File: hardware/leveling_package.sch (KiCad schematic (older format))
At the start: 3 parts, among them J1 Conn_01x16_Male, J2 Conn_01x16_Male

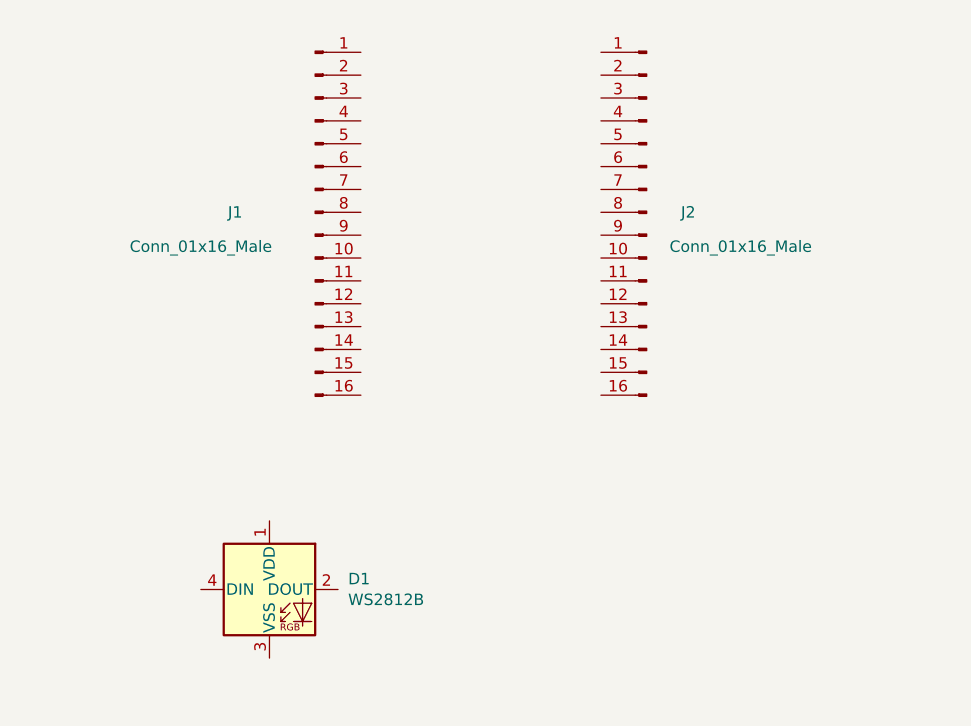
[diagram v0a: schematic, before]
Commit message: first leg with all leds
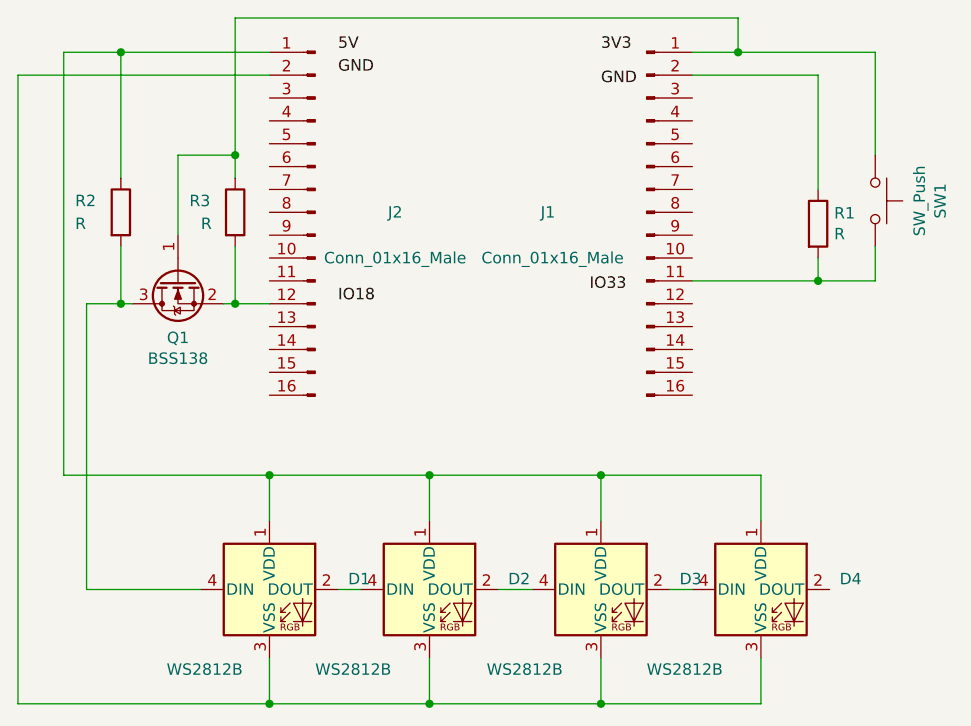
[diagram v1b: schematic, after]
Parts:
- added D2, D3, D4: WS2812B, LED_SMD:LED_WS2812B_PLCC4_5.0x5.0mm_P3.2mm, symbol LED:WS2812B
- added Q1: BSS138, Package_TO_SOT_SMD:SOT-23, symbol Transistor_FET:BSS138
- added R1, R2, R3: R, Resistor_SMD:R_0805_2012Metric_Pad1.15x1.40mm_HandSolder, symbol Device:R
- added SW1: SW_Push, Button_Switch_THT:SW_PUSH_6mm, symbol Switch:SW_Push
- renumbered J2 to J1, J1 to J2
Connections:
- net at J2.1 (Pin_1): now also D1.1 (VDD), D2.1 (VDD), D3.1 (VDD), D4.1 (VDD), R2.1
- net at J2.12 (Pin_12): now also Q1.2 (S), R3.2
- net at J2.2 (Pin_2): now also D1.3 (VSS), D2.3 (VSS), D3.3 (VSS), D4.3 (VSS)
- net at J1.1 (Pin_1): now also Q1.1 (G), R3.1, SW1.1
- net at J1.11 (Pin_11): now also R1.2, SW1.2
- net at J1.2 (Pin_2): now also R1.1
- net at D1.2 (DOUT): now also D2.4 (DIN)
- net at D1.4 (DIN): now also Q1.3 (D), R2.2
- new net: D2.2 (DOUT), D3.4 (DIN)
- new net: D3.2 (DOUT), D4.4 (DIN)
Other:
- moved on the sheet: J1, J2
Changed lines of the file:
@@
 $EndDescr
 $Comp
-L Connector:Conn_01x16_Male J1
+L Connector:Conn_01x16_Male J2
 U 1 1 603EA836
 P 3650 3350
-F 0 "J1" H 3300 3350 50  0000 C CNN
-F 1 "Conn_01x16_Male" H 3150 3200 50  0000 C CNN
+F 0 "J2" H 3300 3350 50  0000 C CNN
+F 1 "Conn_01x16_Male" H 3300 3150 50  0000 C CNN
 F 2 "Connector_PinHeader_2.54mm:PinHeader_1x16_P2.54mm_Vertical" H 3650 3350 50  0001 C CNN
 F 3 "~" H 3650 3350 50  0001 C CNN
 	1    3650 3350
-	1    0    0    -1
-$EndComp
-$Comp
-L Connector:Conn_01x16_Male J2
+	-1   0    0    -1
+$EndComp
+$Comp
+L Connector:Conn_01x16_Male J1
 U 1 1 603ECB79
 P 5100 3350
-F 0 "J2" H 4950 3350 50  0000 R CNN
-F 1 "Conn_01x16_Male" H 5000 3200 50  0000 R CNN
+F 0 "J1" H 4700 3350 50  0000 R CNN
+F 1 "Conn_01x16_Male" H 5000 3150 50  0000 R CNN
 F 2 "Connector_PinHeader_2.54mm:PinHeader_1x16_P2.54mm_Vertical" H 5100 3350 50  0001 C CNN
 F 3 "~" H 5100 3350 50  0001 C CNN
 	1    5100 3350
-	-1   0    0    -1
+	1    0    0    -1
 $EndComp
 $Comp
@@
 P 3450 5000
 F 0 "D1" H 3794 5046 50  0000 L CNN
-F 1 "WS2812B" H 3794 4955 50  0000 L CNN
+F 1 "WS2812B" H 3000 4650 50  0000 L CNN
 F 2 "LED_SMD:LED_WS2812B_PLCC4_5.0x5.0mm_P3.2mm" H 3500 4700 50  0001 L TNN
 F 3 "https://cdn-shop.adafruit.com/datasheets/WS2812B.pdf" H 3550 4625 50  0001 L TNN
@@
 	1    0    0    -1
 $EndComp
+$Comp
+L Switch:SW_Push SW1
+U 1 1 603FB7A3
+P 6100 3300
+F 0 "SW1" H 6100 3585 50  0000 C CNN
+F 1 "SW_Push" H 6100 3494 50  0000 C CNN
+F 2 "Button_Switch_THT:SW_PUSH_6mm" H 6100 3500 50  0001 C CNN
+F 3 "~" H 6100 3500 50  0001 C CNN
+	1    6100 3300
+	0    1    1    0
+$EndComp
+$Comp
+L Device:R R1
+U 1 1 603F0D7F
+P 5850 3400
+F 0 "R1" H 5920 3446 50  0000 L CNN
+F 1 "R" H 5920 3355 50  0000 L CNN
+F 2 "Resistor_SMD:R_0805_2012Metric_Pad1.15x1.40mm_HandSolder" V 5780 3400 50  0001 C CNN
+F 3 "~" H 5850 3400 50  0001 C CNN
+	1    5850 3400
+	1    0    0    -1
+$EndComp
+Wire Wire Line
+	5300 3650 5850 3650
+Wire Wire Line
+	5850 3650 5850 3550
+Wire Wire Line
+	5850 3250 5850 2750
+Wire Wire Line
+	5850 2750 5300 2750
+Wire Wire Line
+	5850 3650 6100 3650
+Wire Wire Line
+	6100 3650 6100 3500
+Connection ~ 5850 3650
+Wire Wire Line
+	6100 3100 6100 2650
+Wire Wire Line
+	6100 2650 5500 2650
+Wire Wire Line
+	3450 4700 3450 4500
+Wire Wire Line
+	3450 4500 2550 4500
+Wire Wire Line
+	2550 4500 2550 2650
+Wire Wire Line
+	2550 2650 2800 2650
+Wire Wire Line
+	3450 5300 3450 5500
+Wire Wire Line
+	3450 5500 2350 5500
+Wire Wire Line
+	2350 5500 2350 2750
+Wire Wire Line
+	2350 2750 3450 2750
+$Comp
+L Transistor_FET:BSS138 Q1
+U 1 1 6040B788
+P 3050 3650
+F 0 "Q1" V 3299 3650 50  0000 C CNN
+F 1 "BSS138" V 3390 3650 50  0000 C CNN
+F 2 "Package_TO_SOT_SMD:SOT-23" H 3250 3575 50  0001 L CIN
+F 3 "https://www.fairchildsemi.com/datasheets/BS/BSS138.pdf" H 3050 3650 50  0001 L CNN
+	1    3050 3650
+	0    -1   1    0
+$EndComp
+Text Label 4900 2650 0    50   ~ 0
+3V3
+Text Label 3750 2650 0    50   ~ 0
+5V
+Text Label 3750 2750 0    50   ~ 0
+GND
+Text Label 4900 2800 0    50   ~ 0
+GND
+Text Label 4850 3700 0    50   ~ 0
+IO33
+Text Label 3750 3750 0    50   ~ 0
+IO18
+Wire Wire Line
+	3450 3750 3300 3750
+Wire Wire Line
+	3150 5000 2650 5000
+Wire Wire Line
+	2650 5000 2650 3750
+Wire Wire Line
+	2650 3750 2800 3750
+$Comp
+L Device:R R3
+U 1 1 6043545A
+P 3300 3350
+F 0 "R3" H 3100 3400 50  0000 L CNN
+F 1 "R" H 3150 3300 50  0000 L CNN
+F 2 "Resistor_SMD:R_0805_2012Metric_Pad1.15x1.40mm_HandSolder" V 3230 3350 50  0001 C CNN
+F 3 "~" H 3300 3350 50  0001 C CNN
+	1    3300 3350
+	1    0    0    -1
+$EndComp
+Wire Wire Line
+	3300 3500 3300 3750
+Connection ~ 3300 3750
+Wire Wire Line
+	3300 3750 3250 3750
+Wire Wire Line
+	3300 3200 3300 3100
+Wire Wire Line
+	3300 2500 5500 2500
+Wire Wire Line
+	5500 2500 5500 2650
+Connection ~ 5500 2650
+Wire Wire Line
+	5500 2650 5300 2650
+Wire Wire Line
+	3300 3100 3050 3100
+Wire Wire Line
+	3050 3100 3050 3450
+Connection ~ 3300 3100
+Wire Wire Line
+	3300 3100 3300 2500
+$Comp
+L Device:R R2
+U 1 1 604443A8
+P 2800 3350
+F 0 "R2" H 2600 3400 50  0000 L CNN
+F 1 "R" H 2600 3300 50  0000 L CNN
+F 2 "Resistor_SMD:R_0805_2012Metric_Pad1.15x1.40mm_HandSolder" V 2730 3350 50  0001 C CNN
+F 3 "~" H 2800 3350 50  0001 C CNN
+	1    2800 3350
+	1    0    0    -1
+$EndComp
+Wire Wire Line
+	2800 3500 2800 3750
+Connection ~ 2800 3750
+Wire Wire Line
+	2800 3750 2850 3750
+Wire Wire Line
+	2800 3200 2800 2650
+Connection ~ 2800 2650
+Wire Wire Line
+	2800 2650 3450 2650
+$Comp
+L LED:WS2812B D2
+U 1 1 60457101
+P 4150 5000
+F 0 "D2" H 4494 5046 50  0000 L CNN
+F 1 "WS2812B" H 3650 4650 50  0000 L CNN
+F 2 "LED_SMD:LED_WS2812B_PLCC4_5.0x5.0mm_P3.2mm" H 4200 4700 50  0001 L TNN
+F 3 "https://cdn-shop.adafruit.com/datasheets/WS2812B.pdf" H 4250 4625 50  0001 L TNN
+	1    4150 5000
+	1    0    0    -1
+$EndComp
+Wire Wire Line
+	3750 5000 3850 5000
+Wire Wire Line
+	3450 5500 4150 5500
+Wire Wire Line
+	4150 5500 4150 5300
+Connection ~ 3450 5500
+Wire Wire Line
+	3450 4500 4150 4500
+Wire Wire Line
+	4150 4500 4150 4700
+Connection ~ 3450 4500
+$Comp
+L LED:WS2812B D3
+U 1 1 6045C053
+P 4900 5000
+F 0 "D3" H 5244 5046 50  0000 L CNN
+F 1 "WS2812B" H 4400 4650 50  0000 L CNN
+F 2 "LED_SMD:LED_WS2812B_PLCC4_5.0x5.0mm_P3.2mm" H 4950 4700 50  0001 L TNN
+F 3 "https://cdn-shop.adafruit.com/datasheets/WS2812B.pdf" H 5000 4625 50  0001 L TNN
+	1    4900 5000
+	1    0    0    -1
+$EndComp
+Wire Wire Line
+	4150 4500 4900 4500
+Wire Wire Line
+	4900 4500 4900 4700
+Connection ~ 4150 4500
+Wire Wire Line
+	4900 5300 4900 5500
+Wire Wire Line
+	4900 5500 4150 5500
+Connection ~ 4150 5500
+Wire Wire Line
+	4450 5000 4600 5000
+$Comp
+L LED:WS2812B D4
+U 1 1 6045F1B5
+P 5600 5000
+F 0 "D4" H 5944 5046 50  0000 L CNN
+F 1 "WS2812B" H 5100 4650 50  0000 L CNN
+F 2 "LED_SMD:LED_WS2812B_PLCC4_5.0x5.0mm_P3.2mm" H 5650 4700 50  0001 L TNN
+F 3 "https://cdn-shop.adafruit.com/datasheets/WS2812B.pdf" H 5700 4625 50  0001 L TNN
+	1    5600 5000
+	1    0    0    -1
+$EndComp
+Wire Wire Line
+	5600 4700 5600 4500
+Wire Wire Line
+	5600 4500 4900 4500
+Connection ~ 4900 4500
+Wire Wire Line
+	5600 5300 5600 5500
+Wire Wire Line
+	5600 5500 4900 5500
+Connection ~ 4900 5500
+Wire Wire Line
+	5200 5000 5300 5000
 $EndSCHEMATC

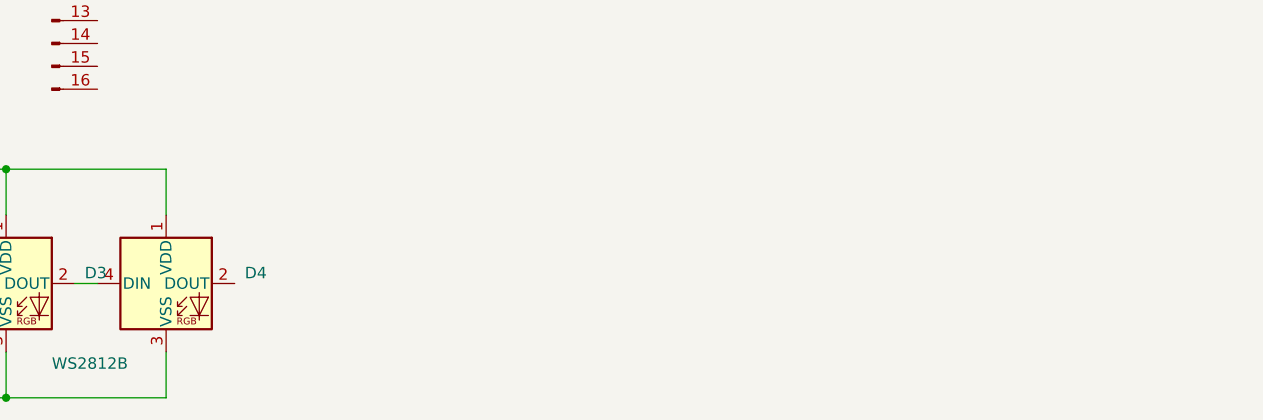
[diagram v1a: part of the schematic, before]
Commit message: all legs with leds
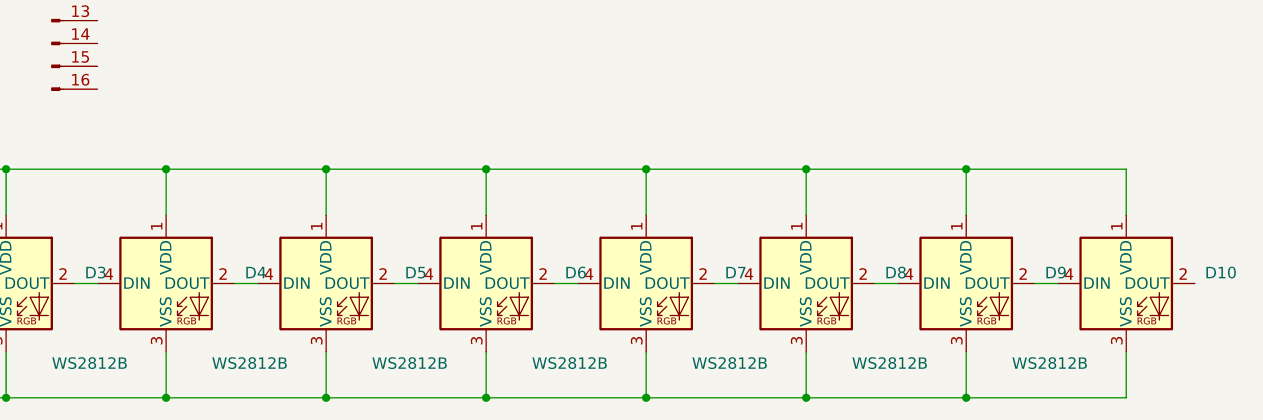
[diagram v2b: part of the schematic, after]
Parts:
- added D10, D5, D6, D7, D8, D9: WS2812B, LED_SMD:LED_WS2812B_PLCC4_5.0x5.0mm_P3.2mm, symbol LED:WS2812B
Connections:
- net at D1.1 (VDD), D2.1 (VDD), D3.1 (VDD)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: now also D10.1 (VDD), D5.1 (VDD), D6.1 (VDD), D7.1 (VDD), D8.1 (VDD), D9.1 (VDD)
- net at D1.3 (VSS), D2.3 (VSS), D3.3 (VSS)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: now also D10.3 (VSS), D5.3 (VSS), D6.3 (VSS), D7.3 (VSS), D8.3 (VSS), D9.3 (VSS)
- net at D4.2 (DOUT): now also D5.4 (DIN)
- new net: D5.2 (DOUT), D6.4 (DIN)
- new net: D6.2 (DOUT), D7.4 (DIN)
- new net: D7.2 (DOUT), D8.4 (DIN)
- new net: D8.2 (DOUT), D9.4 (DIN)
- new net: D10.4 (DIN), D9.2 (DOUT)
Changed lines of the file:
@@
 Wire Wire Line
 	5200 5000 5300 5000
+$Comp
+L LED:WS2812B D5
+U 1 1 604660BC
+P 6300 5000
+F 0 "D5" H 6644 5046 50  0000 L CNN
+F 1 "WS2812B" H 5800 4650 50  0000 L CNN
+F 2 "LED_SMD:LED_WS2812B_PLCC4_5.0x5.0mm_P3.2mm" H 6350 4700 50  0001 L TNN
+F 3 "https://cdn-shop.adafruit.com/datasheets/WS2812B.pdf" H 6400 4625 50  0001 L TNN
+	1    6300 5000
+	1    0    0    -1
+$EndComp
+Wire Wire Line
+	6300 5300 6300 5500
+Wire Wire Line
+	6300 5500 5600 5500
+Connection ~ 5600 5500
+Wire Wire Line
+	6300 4700 6300 4500
+Wire Wire Line
+	6300 4500 5600 4500
+Connection ~ 5600 4500
+Wire Wire Line
+	5900 5000 6000 5000
+$Comp
+L LED:WS2812B D6
+U 1 1 60469B4E
+P 7000 5000
+F 0 "D6" H 7344 5046 50  0000 L CNN
+F 1 "WS2812B" H 6500 4650 50  0000 L CNN
+F 2 "LED_SMD:LED_WS2812B_PLCC4_5.0x5.0mm_P3.2mm" H 7050 4700 50  0001 L TNN
+F 3 "https://cdn-shop.adafruit.com/datasheets/WS2812B.pdf" H 7100 4625 50  0001 L TNN
+	1    7000 5000
+	1    0    0    -1
+$EndComp
+Wire Wire Line
+	7000 4700 7000 4500
+Wire Wire Line
+	7000 4500 6300 4500
+Connection ~ 6300 4500
+Wire Wire Line
+	7000 5500 6300 5500
+Wire Wire Line
+	7000 5300 7000 5500
+Connection ~ 6300 5500
+Wire Wire Line
+	6600 5000 6700 5000
+$Comp
+L LED:WS2812B D7
+U 1 1 6047025A
+P 7700 5000
+F 0 "D7" H 8044 5046 50  0000 L CNN
+F 1 "WS2812B" H 7200 4650 50  0000 L CNN
+F 2 "LED_SMD:LED_WS2812B_PLCC4_5.0x5.0mm_P3.2mm" H 7750 4700 50  0001 L TNN
+F 3 "https://cdn-shop.adafruit.com/datasheets/WS2812B.pdf" H 7800 4625 50  0001 L TNN
+	1    7700 5000
+	1    0    0    -1
+$EndComp
+Wire Wire Line
+	7700 4700 7700 4500
+Wire Wire Line
+	7700 4500 7000 4500
+Connection ~ 7000 4500
+Wire Wire Line
+	7700 5300 7700 5500
+Wire Wire Line
+	7700 5500 7000 5500
+Connection ~ 7000 5500
+Wire Wire Line
+	7300 5000 7400 5000
+$Comp
+L LED:WS2812B D8
+U 1 1 604746C9
+P 8400 5000
+F 0 "D8" H 8744 5046 50  0000 L CNN
+F 1 "WS2812B" H 7900 4650 50  0000 L CNN
+F 2 "LED_SMD:LED_WS2812B_PLCC4_5.0x5.0mm_P3.2mm" H 8450 4700 50  0001 L TNN
+F 3 "https://cdn-shop.adafruit.com/datasheets/WS2812B.pdf" H 8500 4625 50  0001 L TNN
+	1    8400 5000
+	1    0    0    -1
+$EndComp
+Wire Wire Line
+	8400 4700 8400 4500
+Wire Wire Line
+	8400 4500 7700 4500
+Connection ~ 7700 4500
+Wire Wire Line
+	8400 5300 8400 5500
+Wire Wire Line
+	8400 5500 7700 5500
+Connection ~ 7700 5500
+Wire Wire Line
+	8000 5000 8100 5000
+$Comp
+L LED:WS2812B D9
+U 1 1 60480BC4
+P 9100 5000
+F 0 "D9" H 9444 5046 50  0000 L CNN
+F 1 "WS2812B" H 8600 4650 50  0000 L CNN
+F 2 "LED_SMD:LED_WS2812B_PLCC4_5.0x5.0mm_P3.2mm" H 9150 4700 50  0001 L TNN
+F 3 "https://cdn-shop.adafruit.com/datasheets/WS2812B.pdf" H 9200 4625 50  0001 L TNN
+	1    9100 5000
+	1    0    0    -1
+$EndComp
+Wire Wire Line
+	9100 5300 9100 5500
+Wire Wire Line
+	9100 5500 8400 5500
+Connection ~ 8400 5500
+Wire Wire Line
+	9100 4700 9100 4500
+Wire Wire Line
+	9100 4500 8400 4500
+Connection ~ 8400 4500
+Wire Wire Line
+	8700 5000 8800 5000
+$Comp
+L LED:WS2812B D10
+U 1 1 6048635F
+P 9800 5000
+F 0 "D10" H 10144 5046 50  0000 L CNN
+F 1 "WS2812B" H 9300 4650 50  0000 L CNN
+F 2 "LED_SMD:LED_WS2812B_PLCC4_5.0x5.0mm_P3.2mm" H 9850 4700 50  0001 L TNN
+F 3 "https://cdn-shop.adafruit.com/datasheets/WS2812B.pdf" H 9900 4625 50  0001 L TNN
+	1    9800 5000
+	1    0    0    -1
+$EndComp
+Wire Wire Line
+	9800 5300 9800 5500
+Wire Wire Line
+	9800 5500 9100 5500
+Connection ~ 9100 5500
+Wire Wire Line
+	9800 4700 9800 4500
+Wire Wire Line
+	9800 4500 9100 4500
+Connection ~ 9100 4500
+Wire Wire Line
+	9400 5000 9500 5000
 $EndSCHEMATC

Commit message: firmware tests neopix
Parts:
- added D11: WS2812B, LED_SMD:LED_WS2812B_PLCC4_5.0x5.0mm_P3.2mm, symbol LED:WS2812B
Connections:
- net at D1.1 (VDD), D10.1 (VDD), D2.1 (VDD)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: now also D11.1 (VDD)
- net at D1.3 (VSS), D10.3 (VSS), D2.3 (VSS)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: now also D11.3 (VSS)
- net at D10.2 (DOUT): now also D11.4 (DIN)
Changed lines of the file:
@@
 Wire Wire Line
 	9400 5000 9500 5000
+$Comp
+L LED:WS2812B D11
+U 1 1 6041B3FF
+P 10500 5000
+F 0 "D11" H 10844 5046 50  0000 L CNN
+F 1 "WS2812B" H 10000 4650 50  0000 L CNN
+F 2 "LED_SMD:LED_WS2812B_PLCC4_5.0x5.0mm_P3.2mm" H 10550 4700 50  0001 L TNN
+F 3 "https://cdn-shop.adafruit.com/datasheets/WS2812B.pdf" H 10600 4625 50  0001 L TNN
+	1    10500 5000
+	1    0    0    -1
+$EndComp
+Wire Wire Line
+	9800 4500 10500 4500
+Wire Wire Line
+	10500 4500 10500 4700
+Connection ~ 9800 4500
+Wire Wire Line
+	9800 5500 10500 5500
+Wire Wire Line
+	10500 5500 10500 5300
+Connection ~ 9800 5500
+Wire Wire Line
+	10100 5000 10200 5000
 $EndSCHEMATC

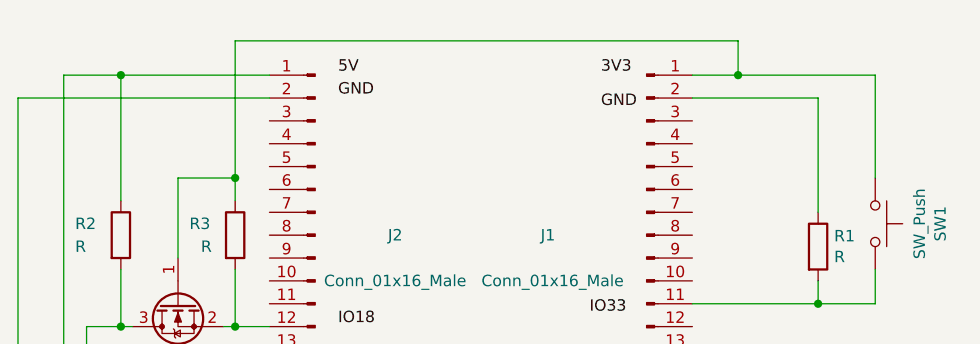
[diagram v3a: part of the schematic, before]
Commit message: legs a bit wider
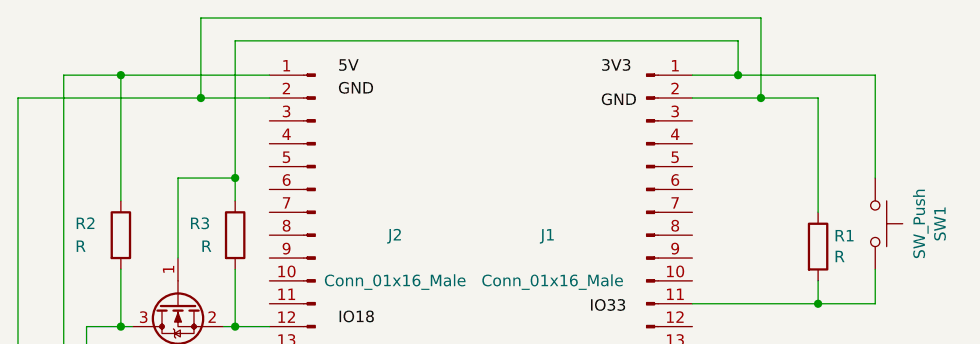
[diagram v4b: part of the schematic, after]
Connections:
- net at D1.3 (VSS), D10.3 (VSS), D11.3 (VSS)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: now also J1.2 (Pin_2), R1.1
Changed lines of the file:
@@
 	5850 3250 5850 2750
 Wire Wire Line
-	5850 2750 5300 2750
+	5850 2750 5600 2750
 Wire Wire Line
 	5850 3650 6100 3650
@@
 	2350 5500 2350 2750
 Wire Wire Line
-	2350 2750 3450 2750
+	2350 2750 3150 2750
 $Comp
 L Transistor_FET:BSS138 Q1
@@
 Wire Wire Line
 	10100 5000 10200 5000
+Wire Wire Line
+	3150 2750 3150 2400
+Wire Wire Line
+	3150 2400 5600 2400
+Wire Wire Line
+	5600 2400 5600 2750
+Connection ~ 3150 2750
+Wire Wire Line
+	3150 2750 3450 2750
+Connection ~ 5600 2750
+Wire Wire Line
+	5600 2750 5300 2750
 $EndSCHEMATC
